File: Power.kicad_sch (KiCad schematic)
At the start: 25 parts, among them Q601 AO3401A, U601 HT7463A, U602 BD2243G, U603 MIC5504-3.3YM5

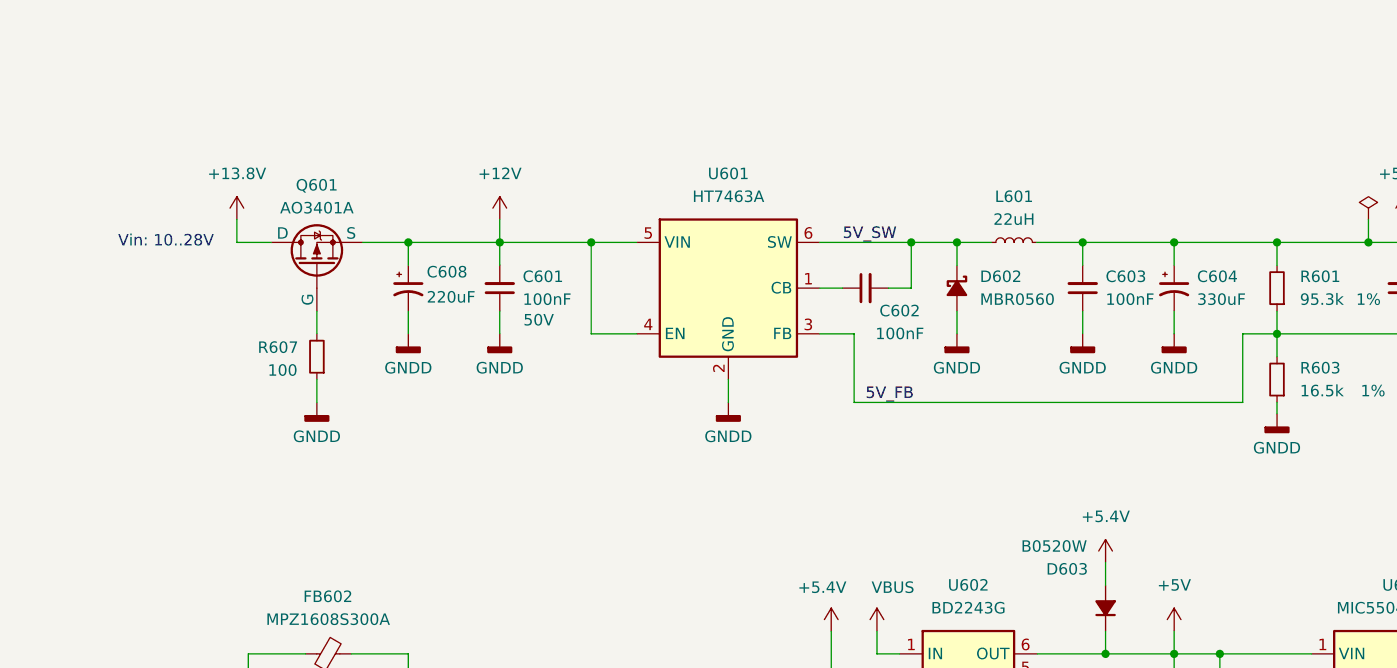
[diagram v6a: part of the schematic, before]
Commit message: Finshed and added revers polarity protection. Improved layout.
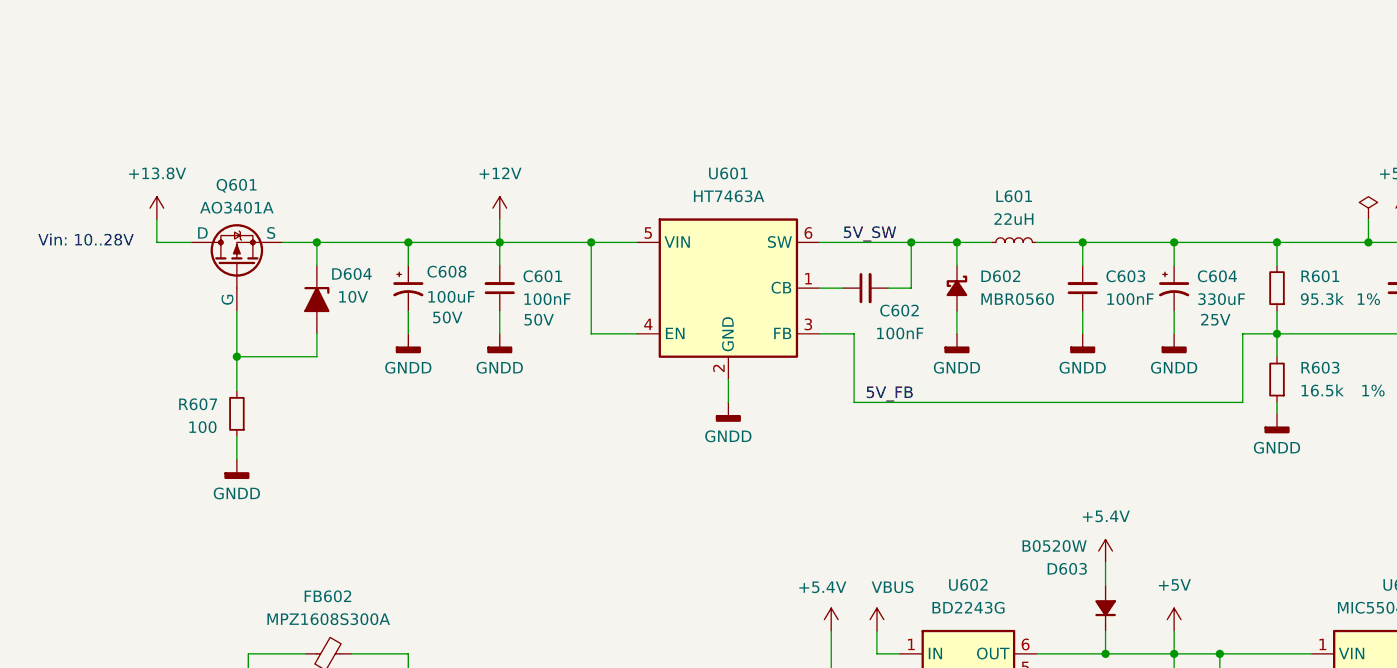
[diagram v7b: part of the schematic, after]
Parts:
- added D604: 10V, Diode_SMD:D_SOD-123, symbol Device:D_Zener_Filled
- C604: footprint Capacitor_THT:CP_Radial_D10.0mm_P5.00mm -> Capacitor_SMD:CP_Elec_6.3x7.7; Manufacturer Panasonic -> KNSCHA; Partnumber EEV-TG1H331Q -> 189RV0016; Voltage 50V -> 25V
- C608: value 220uF -> 100uF; footprint Capacitor_THT:CP_Radial_D10.0mm_P5.00mm -> Capacitor_SMD:CP_Elec_8x10; Manufacturer Panasonic -> Nichicon; Partnumber EEV-TG1H331Q -> UUD1H101MNL1GS
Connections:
- net +12V: now also D604.1 (K)
- net at Q601.2 (G), R607.2: now also D604.2 (A)
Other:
- moved on the sheet: Q601, R607
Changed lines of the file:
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@@
 	)
 	(junction
+		(at 57.15 55.88)
+		(diameter 0)
+		(color 0 0 0 0)
+	)
+	(junction
 		(at 163.83 55.88)
 		(diameter 0)
@@
 	)
 	(junction
+		(at 48.26 68.58)
+		(diameter 0)
+		(color 0 0 0 0)
+	)
+	(junction
 		(at 142.24 55.88)
 		(diameter 0)
@@
 	(wire
 		(pts
+			(xy 57.15 55.88) (xy 57.15 58.42)
+		)
+		(stroke
+			(width 0)
+			(type default)
+		)
+	)
+	(wire
+		(pts
 			(xy 160.02 106.68) (xy 157.48 106.68)
 		)
@@
 	(wire
 		(pts
-			(xy 57.15 63.5) (xy 57.15 66.04)
+			(xy 48.26 63.5) (xy 48.26 68.58)
 		)
 		(stroke
@@
 	(wire
 		(pts
-			(xy 57.15 71.12) (xy 57.15 73.66)
+			(xy 48.26 77.47) (xy 48.26 80.01)
 		)
 		(stroke
@@
 	(wire
 		(pts
+			(xy 57.15 68.58) (xy 48.26 68.58)
+		)
+		(stroke
+			(width 0)
+			(type default)
+		)
+	)
+	(wire
+		(pts
 			(xy 120.65 60.96) (xy 123.19 60.96)
 		)
@@
 	(wire
 		(pts
+			(xy 48.26 68.58) (xy 48.26 72.39)
+		)
+		(stroke
+			(width 0)
+			(type default)
+		)
+	)
+	(wire
+		(pts
 			(xy 142.24 104.14) (xy 142.24 106.68)
 		)
@@
 	(wire
 		(pts
-			(xy 48.26 55.88) (xy 52.07 55.88)
+			(xy 39.37 55.88) (xy 43.18 55.88)
 		)
 		(stroke
@@
 	(wire
 		(pts
-			(xy 48.26 53.34) (xy 48.26 55.88)
+			(xy 39.37 53.34) (xy 39.37 55.88)
 		)
 		(stroke
@@
 	(wire
 		(pts
-			(xy 62.23 55.88) (xy 67.31 55.88)
+			(xy 53.34 55.88) (xy 57.15 55.88)
 		)
 		(stroke
@@
 	(wire
 		(pts
+			(xy 57.15 66.04) (xy 57.15 68.58)
+		)
+		(stroke
+			(width 0)
+			(type default)
+		)
+	)
+	(wire
+		(pts
 			(xy 177.8 63.5) (xy 177.8 66.04)
 		)
@@
 	(wire
 		(pts
+			(xy 57.15 55.88) (xy 67.31 55.88)
+		)
+		(stroke
+			(width 0)
+			(type default)
+		)
+	)
+	(wire
+		(pts
 			(xy 129.54 111.76) (xy 129.54 114.3)
 		)
@@
 	(text "Vin: 10..28V"
 		(exclude_from_sim no)
-		(at 40.386 55.88 0)
+		(at 31.496 55.88 0)
 		(effects
 			(font
@@
 			)
 		)
-		(property "Value" "220uF"
+		(property "Value" "100uF"
 			(at 69.342 61.976 0)
 			(effects
@@
 			)
 		)
-		(property "Footprint" "Capacitor_THT:CP_Radial_D10.0mm_P5.00mm"
+		(property "Footprint" "Capacitor_SMD:CP_Elec_8x10"
 			(at 67.31 60.96 0)
 			(effects
@@
 			)
 		)
-		(property "Manufacturer" "Panasonic"
+		(property "Manufacturer" "Nichicon"
 			(at 67.31 60.96 0)
 			(effects
@@
 			)
 		)
-		(property "Partnumber" "EEV-TG1H331Q"
+		(property "Partnumber" "UUD1H101MNL1GS"
 			(at 67.31 60.96 0)
 			(effects
@@
 		)
 		(property "Voltage" "50V"
-			(at 67.31 60.96 0)
+			(at 71.628 64.262 0)
 			(effects
 				(font
 					(size 1.27 1.27)
 				)
-				(hide yes)
 			)
 		)
@@
 	)
 	(symbol
+		(lib_id "Device:D_Zener_Filled")
+		(at 57.15 62.23 270)
+		(unit 1)
+		(exclude_from_sim no)
+		(in_bom yes)
+		(on_board yes)
+		(dnp no)
+		(property "Reference" "D604"
+			(at 58.674 59.436 90)
+			(effects
+				(font
+					(size 1.27 1.27)
+				)
+				(justify left)
+			)
+		)
+		(property "Value" "10V"
+			(at 59.436 61.976 90)
+			(effects
+				(font
+					(size 1.27 1.27)
+				)
+				(justify left)
+			)
+		)
+		(property "Footprint" "Diode_SMD:D_SOD-123"
+			(at 57.15 62.23 0)
+			(effects
+				(font
+					(size 1.27 1.27)
+				)
+				(hide yes)
+			)
+		)
+		(property "Datasheet" "~"
+			(at 57.15 62.23 0)
+			(effects
+				(font
+					(size 1.27 1.27)
+				)
+				(hide yes)
+			)
+		)
+		(property "Description" "Zener diode, filled shape"
+			(at 57.15 62.23 0)
+			(effects
+				(font
+					(size 1.27 1.27)
+				)
+				(hide yes)
+			)
+		)
+		(property "Partnumber" "BZT52C10"
+			(at 57.15 62.23 90)
+			(effects
+				(font
+					(size 1.27 1.27)
+				)
+				(hide yes)
+			)
+		)
+		(pin "2"
+		)
+		(pin "1"
+		)
+		(instances
+			(project "ZFTuner"
+				(path "/fdb95973-bff7-44bf-8fa0-11fcc1e3382d/4f4b3f21-035d-41e9-bc50-b9de10321df3"
+					(reference "D604")
+					(unit 1)
+				)
+			)
+		)
+	)
+	(symbol
 		(lib_id "Simulation_SPICE:PMOS")
-		(at 57.15 58.42 90)
+		(at 48.26 58.42 90)
 		(unit 1)
 		(exclude_from_sim no)
@@
 		(dnp no)
 		(property "Reference" "Q601"
-			(at 57.15 49.53 90)
+			(at 48.26 49.53 90)
 			(effects
 				(font
@@
 		)
 		(property "Value" "AO3401A"
-			(at 57.15 52.07 90)
+			(at 48.26 52.07 90)
 			(effects
 				(font
@@
 		)
 		(property "Footprint" "Package_TO_SOT_SMD:SOT-23"
-			(at 54.61 53.34 0)
+			(at 45.72 53.34 0)
 			(effects
 				(font
@@
 		)
 		(property "Datasheet" "~"
-			(at 69.85 58.42 0)
+			(at 60.96 58.42 0)
 			(effects
 				(font
@@
 		)
 		(property "Description" "P-MOSFET transistor, drain/source/gate"
-			(at 57.15 58.42 0)
+			(at 48.26 58.42 0)
 			(effects
 				(font
@@
 		)
 		(property "Sim.Device" "PMOS"
-			(at 74.295 58.42 0)
+			(at 65.405 58.42 0)
 			(effects
 				(font
@@
 		)
 		(property "Sim.Type" "VDMOS"
-			(at 76.2 58.42 0)
+			(at 67.31 58.42 0)
 			(effects
 				(font
@@
 		)
 		(property "Sim.Pins" "1=D 2=G 3=S"
-			(at 72.39 58.42 0)
+			(at 63.5 58.42 0)
 			(effects
 				(font
@@
 		(on_board yes)
 		(dnp no)
-		(fields_autoplaced yes)
 		(property "Reference" "C604"
 			(at 154.94 59.6899 0)
@@
 			)
 		)
-		(property "Footprint" "Capacitor_THT:CP_Radial_D10.0mm_P5.00mm"
+		(property "Footprint" "Capacitor_SMD:CP_Elec_6.3x7.7"
 			(at 152.4 60.96 0)
 			(effects
@@
 			)
 		)
-		(property "Manufacturer" "Panasonic"
+		(property "Manufacturer" "KNSCHA"
 			(at 152.4 60.96 0)
 			(effects
@@
 			)
 		)
-		(property "Partnumber" "EEV-TG1H331Q"
+		(property "Partnumber" "189RV0016"
 			(at 152.4 60.96 0)
 			(effects
@@
 			)
 		)
-		(property "Voltage" "50V"
-			(at 152.4 60.96 0)
+		(property "Voltage" "25V"
+			(at 156.972 64.516 0)
 			(effects
 				(font
 					(size 1.27 1.27)
 				)
-				(hide yes)
 			)
 		)
@@
 	(symbol
 		(lib_id "power:GNDD")
-		(at 57.15 73.66 0)
+		(at 48.26 80.01 0)
 		(unit 1)
 		(exclude_from_sim no)
@@
 		(fields_autoplaced yes)
 		(property "Reference" "#PWR0617"
-			(at 57.15 80.01 0)
+			(at 48.26 86.36 0)
 			(effects
 				(font
@@
 		)
 		(property "Value" "GNDD"
-			(at 57.15 77.47 0)
+			(at 48.26 83.82 0)
 			(effects
 				(font
@@
 		)
 		(property "Footprint" ""
-			(at 57.15 73.66 0)
+			(at 48.26 80.01 0)
 			(effects
 				(font
@@
 		)
 		(property "Datasheet" ""
-			(at 57.15 73.66 0)
+			(at 48.26 80.01 0)
 			(effects
 				(font
@@
 		)
 		(property "Description" "Power symbol creates a global label with name \"GNDD\" , digital ground"
-			(at 57.15 73.66 0)
+			(at 48.26 80.01 0)
 			(effects
 				(font
@@
 	(symbol
 		(lib_id "power:+12V")
-		(at 48.26 53.34 0)
+		(at 39.37 53.34 0)
 		(unit 1)
 		(exclude_from_sim no)
@@
 		(fields_autoplaced yes)
 		(property "Reference" "#PWR0626"
-			(at 48.26 57.15 0)
+			(at 39.37 57.15 0)
 			(effects
 				(font
@@
 		)
 		(property "Value" "+13.8V"
-			(at 48.26 48.26 0)
+			(at 39.37 48.26 0)
 			(effects
 				(font
@@
 		)
 		(property "Footprint" ""
-			(at 48.26 53.34 0)
+			(at 39.37 53.34 0)
 			(effects
 				(font
@@
 		)
 		(property "Datasheet" ""
-			(at 48.26 53.34 0)
+			(at 39.37 53.34 0)
 			(effects
 				(font
@@
 		)
 		(property "Description" "Power symbol creates a global label with name \"+12V\""
-			(at 48.26 53.34 0)
+			(at 39.37 53.34 0)
 			(effects
 				(font
@@
 	(symbol
 		(lib_id "Device:R_Small")
-		(at 57.15 68.58 180)
+		(at 48.26 74.93 180)
 		(unit 1)
 		(exclude_from_sim no)
@@
 		(dnp no)
 		(property "Reference" "R607"
-			(at 52.832 67.564 0)
+			(at 43.942 73.914 0)
 			(effects
 				(font
@@
 		)
 		(property "Value" "100"
-			(at 53.34 70.104 0)
+			(at 44.45 76.454 0)
 			(effects
 				(font
@@
 		)
 		(property "Footprint" "Resistor_SMD:R_0603_1608Metric"
-			(at 57.15 68.58 0)
+			(at 48.26 74.93 0)
 			(effects
 				(font
@@
 		)
 		(property "Datasheet" "~"
-			(at 57.15 68.58 0)
+			(at 48.26 74.93 0)
 			(effects
 				(font
@@
 		)
 		(property "Description" "Resistor, small symbol"
-			(at 57.15 68.58 0)
+			(at 48.26 74.93 0)
 			(effects
 				(font

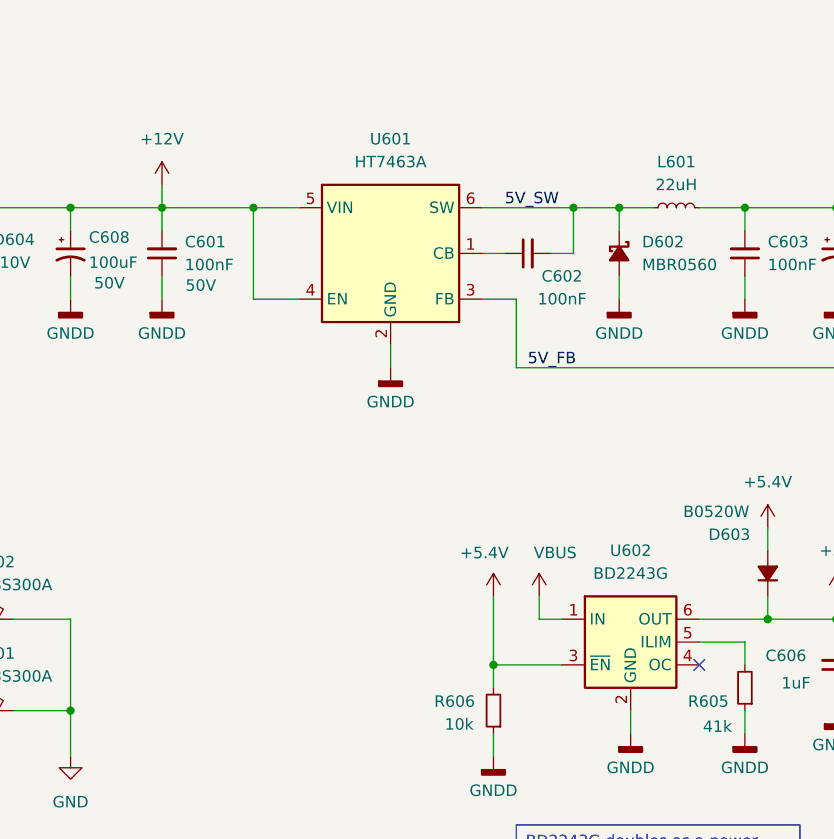
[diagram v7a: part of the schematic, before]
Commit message: Minor schematic fixes
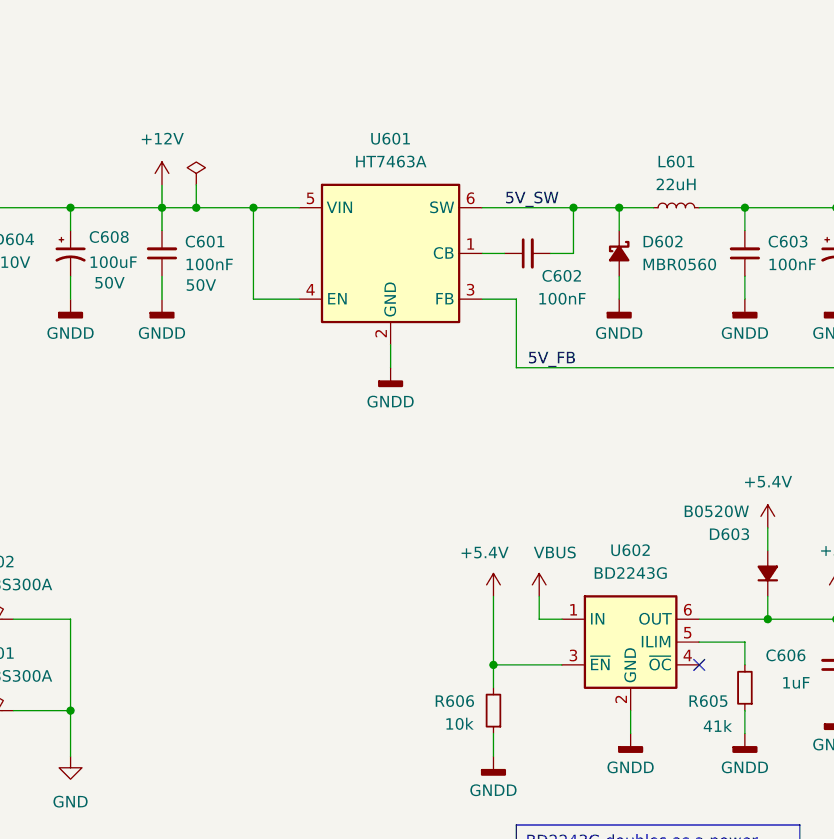
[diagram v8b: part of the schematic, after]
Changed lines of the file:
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@@
 	)
 	(junction
+		(at 81.28 55.88)
+		(diameter 0)
+		(color 0 0 0 0)
+	)
+	(junction
 		(at 67.31 55.88)
 		(diameter 0)
@@
 	(wire
 		(pts
+			(xy 81.28 55.88) (xy 87.63 55.88)
+		)
+		(stroke
+			(width 0)
+			(type solid)
+		)
+	)
+	(wire
+		(pts
 			(xy 160.02 106.68) (xy 157.48 106.68)
 		)
@@
 	(wire
 		(pts
-			(xy 77.47 55.88) (xy 87.63 55.88)
+			(xy 77.47 55.88) (xy 81.28 55.88)
 		)
 		(stroke
@@
 	(wire
 		(pts
+			(xy 81.28 53.34) (xy 81.28 55.88)
+		)
+		(stroke
+			(width 0)
+			(type default)
+		)
+	)
+	(wire
+		(pts
 			(xy 116.84 66.04) (xy 113.03 66.04)
 		)
@@
 			)
 		)
-		(property "Description" "Adjustable current limit high side switch IC, 2.8..5.5V, 0.2..1.7A"
+		(property "Description" "Adjustable current limit high side switch IC, active-low enable, output discharge, 2.8..5.5V, 0.2..1.7A, 89mOhm Ron, TSOP-6"
 			(at 129.54 120.904 0)
 			(effects
@@
 					(unit 1)
 				)
+			)
+		)
+	)
+	(symbol
+		(lib_id "power:PWR_FLAG")
+		(at 81.28 53.34 0)
+		(unit 1)
+		(exclude_from_sim no)
+		(in_bom yes)
+		(on_board yes)
+		(dnp no)
+		(fields_autoplaced yes)
+		(property "Reference" "#FLG0602"
+			(at 81.28 51.435 0)
+			(effects
+				(font
+					(size 1.27 1.27)
+				)
+				(hide yes)
+			)
+		)
+		(property "Value" "PWR_FLAG"
+			(at 81.28 48.26 0)
+			(effects
+				(font
+					(size 1.27 1.27)
+				)
+				(hide yes)
+			)
+		)
+		(property "Footprint" ""
+			(at 81.28 53.34 0)
+			(effects
+				(font
+					(size 1.27 1.27)
+				)
+				(hide yes)
+			)
+		)
+		(property "Datasheet" "~"
+			(at 81.28 53.34 0)
+			(effects
+				(font
+					(size 1.27 1.27)
+				)
+				(hide yes)
+			)
+		)
+		(property "Description" "Special symbol for telling ERC where power comes from"
+			(at 81.28 53.34 0)
+			(effects
+				(font
+					(size 1.27 1.27)
+				)
+				(hide yes)
+			)
+		)
+		(pin "1"
+		)
+		(instances
+			(project "ZFTuner"
+				(path "/fdb95973-bff7-44bf-8fa0-11fcc1e3382d/4f4b3f21-035d-41e9-bc50-b9de10321df3"
+					(reference "#FLG0602")
+					(unit 1)
+				)
